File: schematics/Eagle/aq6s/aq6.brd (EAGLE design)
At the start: 99.8 x 66.8 mm, 24 parts

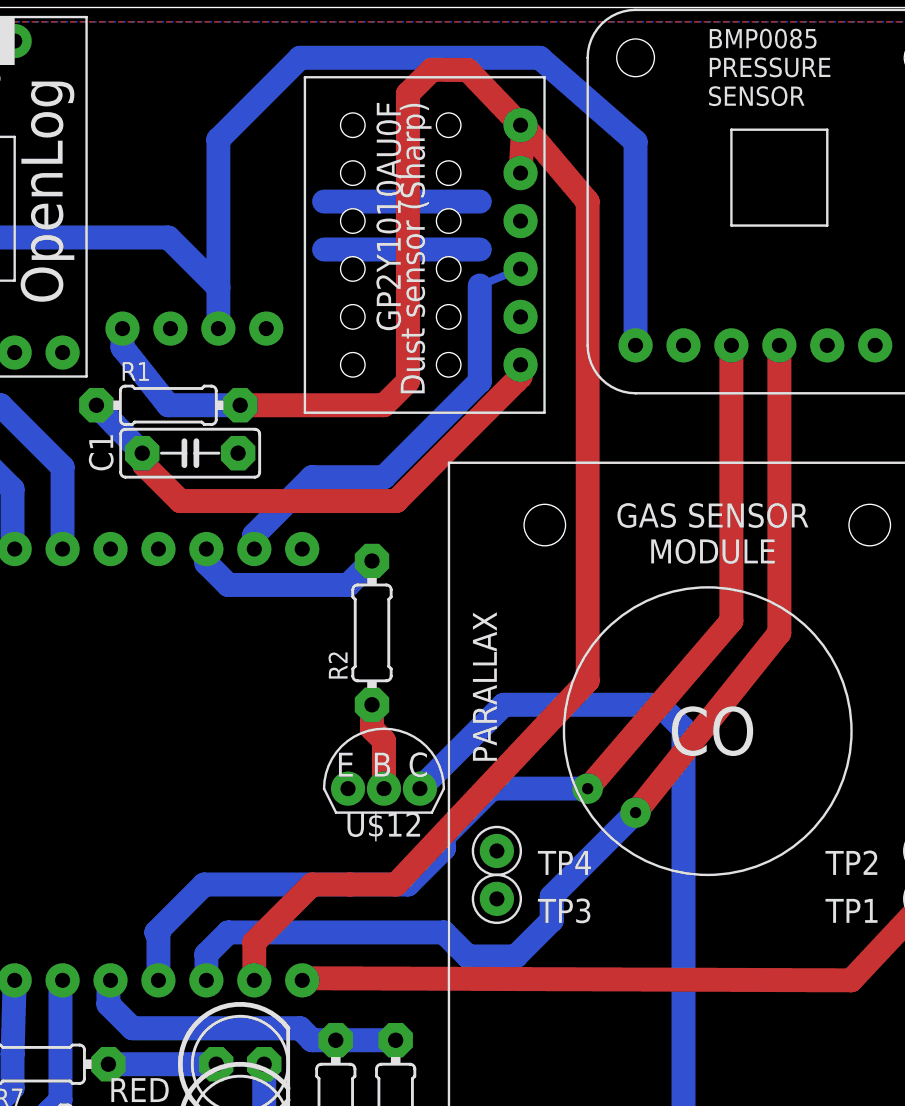
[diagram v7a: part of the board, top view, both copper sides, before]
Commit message: Fixed pcb, reexport to png! Update Ard. code
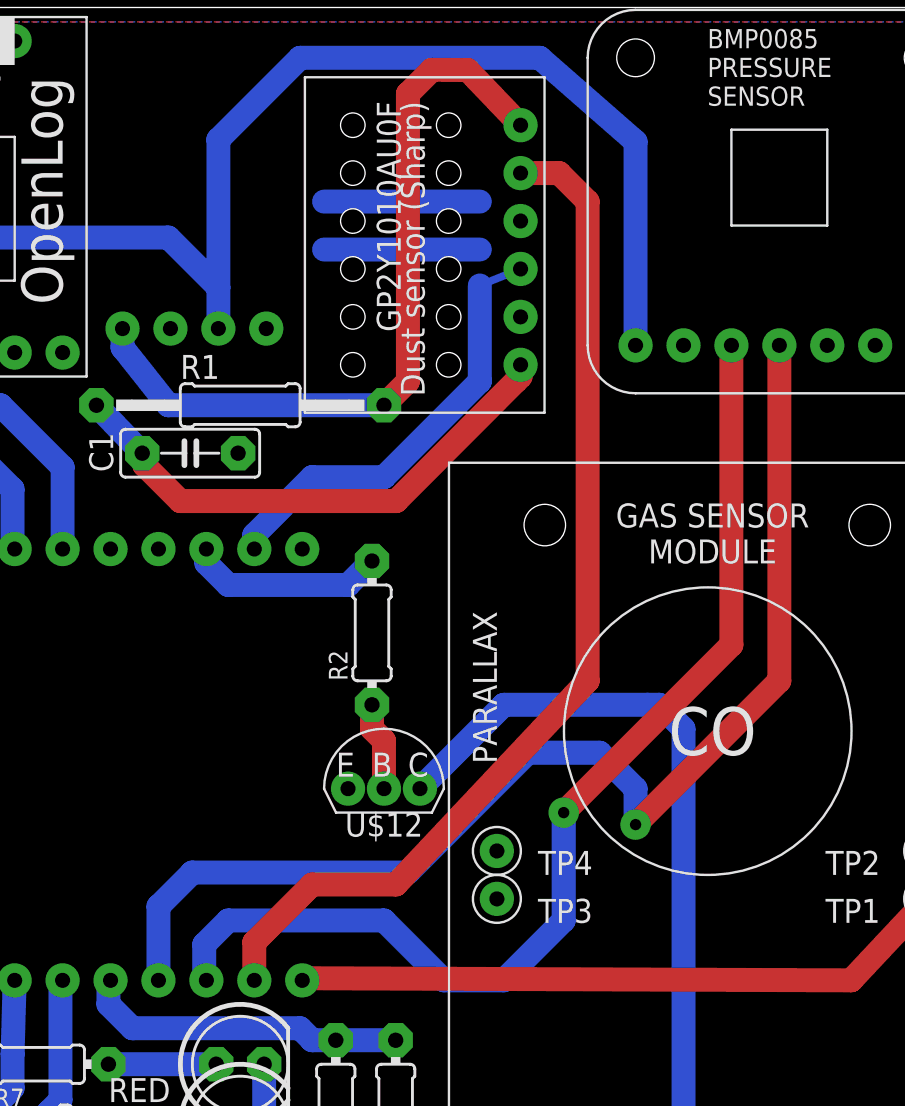
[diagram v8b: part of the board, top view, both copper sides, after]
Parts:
- R1: device resistor:0204/7 -> rcl:0207/15
- moved R1 3.81 mm to (61.0, 45.7)
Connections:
- removed net N$24: U$2.A5, U$8.SDA
- new net N$22: U$2.A4, U$8.SDA
- net N$23: now also U$2.A5; no longer U$2.A4
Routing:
- net N$22: track 0.00 -> 63.8 mm, vias 0 -> 1
- net N$24: track 56.5 -> 0.00 mm, vias 1 -> 0
- net N$3: track 58.9 -> 55.2 mm
- net N$23: track 55.3 -> 58.3 mm
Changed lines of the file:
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@@
 <attribute name="VALUE" x="62.499" y="42.291" size="1.27" layer="27" ratio="10"/>
 </element>
-<element name="R1" library="resistor" package="0204/7" value="150Ω" x="57.15" y="45.72"/>
+<element name="R1" library="rcl" package="0207/15" value="150Ω" x="60.96" y="45.72"/>
 <element name="U$3" library="air_quality_parts" package="POLOLU_VAR_VOLTAGE_REG" value="POLOLU_VAR_VOLTAGE_REG" x="58.532" y="56.134" rot="MR0"/>
 <element name="U$4" library="air_quality_parts" package="ADAFRUIT_GPS_V3" value="ADAFRUIT_GPS_V3" x="34.275" y="41.148" rot="R90"/>
@@
 <contactref element="U$3" pad="P$4"/>
 <contactref element="R1" pad="2"/>
-<wire x1="60.96" y1="45.72" x2="68.58" y2="45.72" width="1.27" layer="1"/>
 <wire x1="68.58" y1="45.72" x2="69.85" y2="46.99" width="1.27" layer="1"/>
 <wire x1="69.85" y1="46.99" x2="69.85" y2="62.23" width="1.27" layer="1"/>
@@
 <wire x1="54.722" y1="49.784" x2="54.722" y2="48.783" width="1.27" layer="16"/>
 <wire x1="54.722" y1="48.783" x2="57.15" y2="45.72" width="1.27" layer="16"/>
-<wire x1="57.15" y1="45.72" x2="60.96" y2="45.72" width="1.27" layer="16"/>
+<wire x1="57.15" y1="45.72" x2="68.58" y2="45.72" width="1.27" layer="16"/>
 </signal>
 <signal name="N$2">
@@
 <contactref element="U$1" pad="P$5"/>
 <contactref element="U$2" pad="A6"/>
-<wire x1="75.819" y1="58.024" x2="75.961" y2="60.564" width="1.27" layer="1"/>
-<wire x1="75.961" y1="60.564" x2="79.375" y2="56.515" width="1.27" layer="1"/>
 <wire x1="79.375" y1="56.515" x2="79.375" y2="31.115" width="1.27" layer="1"/>
 <wire x1="79.375" y1="31.115" x2="69.215" y2="20.32" width="1.27" layer="1"/>
-<wire x1="69.215" y1="20.32" x2="66.787" y2="20.32" width="1.27" layer="1"/>
-<wire x1="66.787" y1="20.32" x2="64.77" y2="20.32" width="1.27" layer="1"/>
-<wire x1="64.77" y1="20.32" x2="62.23" y2="17.78" width="1.27" layer="1"/>
-<wire x1="62.23" y1="17.78" x2="61.707" y2="17.257" width="1.27" layer="1"/>
+<wire x1="69.215" y1="20.32" x2="64.77" y2="20.32" width="1.27" layer="1"/>
+<wire x1="64.77" y1="20.32" x2="61.707" y2="17.257" width="1.27" layer="1"/>
 <wire x1="61.707" y1="17.257" x2="61.707" y2="15.24" width="1.27" layer="1"/>
+<wire x1="75.819" y1="58.024" x2="77.866" y2="58.024" width="1.27" layer="1"/>
+<wire x1="77.866" y1="58.024" x2="79.375" y2="56.515" width="1.27" layer="1"/>
 </signal>
 <signal name="N$4">
@@
 <signal name="N$23">
 <contactref element="U$8" pad="SCL"/>
-<contactref element="U$2" pad="A4"/>
-<wire x1="56.627" y1="15.24" x2="56.627" y2="17.668" width="1.27" layer="16"/>
-<wire x1="56.627" y1="17.668" x2="56.515" y2="17.78" width="1.27" layer="16"/>
-<wire x1="56.515" y1="17.78" x2="59.055" y2="20.32" width="1.27" layer="16"/>
-<wire x1="59.055" y1="20.32" x2="69.85" y2="20.32" width="1.27" layer="16"/>
-<wire x1="69.85" y1="20.32" x2="71.755" y2="22.225" width="1.27" layer="16"/>
-<wire x1="71.755" y1="22.225" x2="71.755" y2="22.86" width="1.27" layer="16"/>
-<wire x1="71.755" y1="22.86" x2="74.295" y2="25.4" width="1.27" layer="16"/>
-<wire x1="74.295" y1="25.4" x2="79.375" y2="25.4" width="1.27" layer="16"/>
-<wire x1="86.995" y1="48.895" x2="86.995" y2="34.29" width="1.27" layer="1"/>
-<wire x1="86.995" y1="34.29" x2="79.375" y2="25.4" width="1.27" layer="1"/>
-<via x="79.375" y="25.4" extent="1-16" drill="0.6" shape="square"/>
-</signal>
-<signal name="N$24">
-<contactref element="U$8" pad="SDA"/>
 <contactref element="U$2" pad="A5"/>
-<wire x1="89.535" y1="48.895" x2="89.535" y2="33.655" width="1.27" layer="1"/>
-<via x="81.915" y="24.13" extent="1-16" drill="0.6" shape="square"/>
-<wire x1="89.535" y1="33.655" x2="81.915" y2="24.13" width="1.27" layer="1"/>
-<wire x1="81.915" y1="24.13" x2="77.47" y2="19.685" width="1.27" layer="16"/>
-<wire x1="77.47" y1="19.685" x2="77.47" y2="18.415" width="1.27" layer="16"/>
-<wire x1="77.47" y1="18.415" x2="75.565" y2="16.51" width="1.27" layer="16"/>
-<wire x1="75.565" y1="16.51" x2="73.025" y2="16.51" width="1.27" layer="16"/>
-<wire x1="73.025" y1="16.51" x2="71.755" y2="17.78" width="1.27" layer="16"/>
-<wire x1="71.755" y1="17.78" x2="60.325" y2="17.78" width="1.27" layer="16"/>
-<wire x1="60.325" y1="17.78" x2="59.167" y2="16.622" width="1.27" layer="16"/>
-<wire x1="59.167" y1="16.622" x2="59.167" y2="15.24" width="1.27" layer="16"/>
+<wire x1="86.995" y1="48.895" x2="86.995" y2="33.02" width="1.27" layer="1"/>
+<wire x1="86.995" y1="33.02" x2="78.105" y2="24.13" width="1.27" layer="1"/>
+<via x="78.105" y="24.13" extent="1-16" drill="0.6" shape="square"/>
+<wire x1="78.105" y1="24.13" x2="78.105" y2="18.415" width="1.27" layer="16"/>
+<wire x1="78.105" y1="18.415" x2="74.93" y2="15.24" width="1.27" layer="16"/>
+<wire x1="74.93" y1="15.24" x2="71.755" y2="15.24" width="1.27" layer="16"/>
+<wire x1="71.755" y1="15.24" x2="68.58" y2="18.415" width="1.27" layer="16"/>
+<wire x1="68.58" y1="18.415" x2="60.325" y2="18.415" width="1.27" layer="16"/>
+<wire x1="60.325" y1="18.415" x2="59.055" y2="17.145" width="1.27" layer="16"/>
+<wire x1="59.055" y1="17.145" x2="59.055" y2="15.352" width="1.27" layer="16"/>
+<wire x1="59.055" y1="15.352" x2="59.167" y2="15.24" width="1.27" layer="16"/>
 </signal>
 <signal name="N$6">
@@
 <wire x1="51.435" y1="15.128" x2="51.547" y2="15.24" width="1.27" layer="16"/>
 </signal>
+<signal name="N$22">
+<contactref element="U$8" pad="SDA"/>
+<contactref element="U$2" pad="A4"/>
+<wire x1="89.535" y1="48.895" x2="89.535" y2="31.115" width="1.27" layer="1"/>
+<wire x1="89.535" y1="31.115" x2="81.915" y2="23.495" width="1.27" layer="1"/>
+<via x="81.915" y="23.495" extent="1-16" drill="0.6" shape="square"/>
+<wire x1="56.627" y1="15.24" x2="56.627" y2="19.162" width="1.27" layer="16"/>
+<wire x1="56.627" y1="19.162" x2="58.42" y2="20.955" width="1.27" layer="16"/>
+<wire x1="58.42" y1="20.955" x2="69.85" y2="20.955" width="1.27" layer="16"/>
+<wire x1="69.85" y1="20.955" x2="76.2" y2="27.305" width="1.27" layer="16"/>
+<wire x1="76.2" y1="27.305" x2="80.01" y2="27.305" width="1.27" layer="16"/>
+<wire x1="80.01" y1="27.305" x2="81.915" y2="25.4" width="1.27" layer="16"/>
+<wire x1="81.915" y1="25.4" x2="81.915" y2="23.495" width="1.27" layer="16"/>
+</signal>
 </signals>
